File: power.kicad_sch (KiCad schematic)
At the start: 5 parts, among them U3 TCR2EF36, U4 MIC5365-3.0YD5-TR

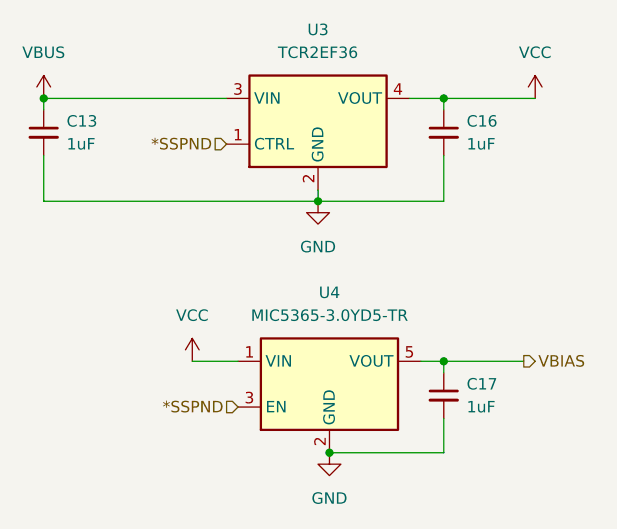
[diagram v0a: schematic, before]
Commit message: Add missing PCM2906 components; Partially Implement PCB
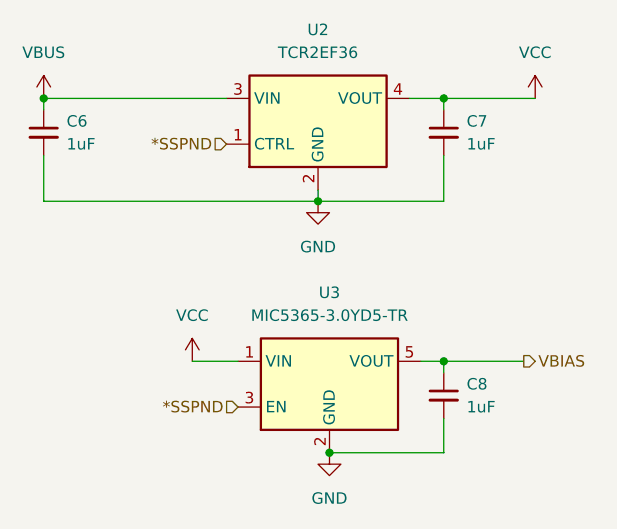
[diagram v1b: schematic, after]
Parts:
- C6: renamed from C13; footprint (none) -> Capacitor_SMD:C_0603_1608Metric_Pad1.08x0.95mm_HandSolder
- C7: renamed from C16; footprint (none) -> Capacitor_SMD:C_0603_1608Metric_Pad1.08x0.95mm_HandSolder
- C8: renamed from C17; footprint (none) -> Capacitor_SMD:C_0603_1608Metric_Pad1.08x0.95mm_HandSolder
- renumbered U3 to U2, U4 to U3
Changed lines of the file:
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@@
 		(dnp no)
 		(fields_autoplaced yes)
-		(property "Reference" "U3"
+		(property "Reference" "U2"
 			(at 132.08 92.71 0)
 			(effects
@@
 			(project ""
 				(path "/eb1afd54-626c-4526-850f-b0511eb9dc59/b6fbeffe-7e55-4f10-a8ab-72b4928b7916"
-					(reference "U3")
+					(reference "U2")
 					(unit 1)
 				)
@@
 		(dnp no)
 		(fields_autoplaced yes)
-		(property "Reference" "#PWR08"
+		(property "Reference" "#PWR07"
 			(at 118.11 133.35 0)
 			(effects
@@
 			(project ""
 				(path "/eb1afd54-626c-4526-850f-b0511eb9dc59/b6fbeffe-7e55-4f10-a8ab-72b4928b7916"
-					(reference "#PWR08")
+					(reference "#PWR07")
 					(unit 1)
 				)
@@
 		(dnp no)
 		(fields_autoplaced yes)
-		(property "Reference" "U4"
+		(property "Reference" "U3"
 			(at 133.35 121.92 0)
 			(effects
@@
 			(project ""
 				(path "/eb1afd54-626c-4526-850f-b0511eb9dc59/b6fbeffe-7e55-4f10-a8ab-72b4928b7916"
-					(reference "U4")
+					(reference "U3")
 					(unit 1)
 				)
@@
 		(dnp no)
 		(fields_autoplaced yes)
-		(property "Reference" "C13"
+		(property "Reference" "C6"
 			(at 104.14 102.8762 0)
 			(effects
@@
 			)
 		)
-		(property "Footprint" ""
+		(property "Footprint" "Capacitor_SMD:C_0603_1608Metric_Pad1.08x0.95mm_HandSolder"
 			(at 101.6 104.14 0)
 			(effects
@@
 			(project "lesson2"
 				(path "/eb1afd54-626c-4526-850f-b0511eb9dc59/b6fbeffe-7e55-4f10-a8ab-72b4928b7916"
-					(reference "C13")
+					(reference "C6")
 					(unit 1)
 				)
@@
 		(dnp no)
 		(fields_autoplaced yes)
-		(property "Reference" "C17"
+		(property "Reference" "C8"
 			(at 148.59 132.0862 0)
 			(effects
@@
 			)
 		)
-		(property "Footprint" ""
+		(property "Footprint" "Capacitor_SMD:C_0603_1608Metric_Pad1.08x0.95mm_HandSolder"
 			(at 146.05 133.35 0)
 			(effects
@@
 			(project ""
 				(path "/eb1afd54-626c-4526-850f-b0511eb9dc59/b6fbeffe-7e55-4f10-a8ab-72b4928b7916"
-					(reference "C17")
+					(reference "C8")
 					(unit 1)
 				)
@@
 		(dnp no)
 		(fields_autoplaced yes)
-		(property "Reference" "C16"
+		(property "Reference" "C7"
 			(at 148.59 102.8762 0)
 			(effects
@@
 			)
 		)
-		(property "Footprint" ""
+		(property "Footprint" "Capacitor_SMD:C_0603_1608Metric_Pad1.08x0.95mm_HandSolder"
 			(at 146.05 104.14 0)
 			(effects
@@
 			(project "lesson2"
 				(path "/eb1afd54-626c-4526-850f-b0511eb9dc59/b6fbeffe-7e55-4f10-a8ab-72b4928b7916"
-					(reference "C16")
+					(reference "C7")
 					(unit 1)
 				)
@@
 		(dnp no)
 		(fields_autoplaced yes)
-		(property "Reference" "#PWR07"
+		(property "Reference" "#PWR09"
 			(at 133.35 146.05 0)
 			(effects
@@
 			(project ""
 				(path "/eb1afd54-626c-4526-850f-b0511eb9dc59/b6fbeffe-7e55-4f10-a8ab-72b4928b7916"
-					(reference "#PWR07")
+					(reference "#PWR09")
 					(unit 1)
 				)
@@
 		(dnp no)
 		(fields_autoplaced yes)
-		(property "Reference" "#PWR09"
+		(property "Reference" "#PWR08"
 			(at 132.08 118.11 0)
 			(effects
@@
 			(project "lesson2"
 				(path "/eb1afd54-626c-4526-850f-b0511eb9dc59/b6fbeffe-7e55-4f10-a8ab-72b4928b7916"
-					(reference "#PWR09")
+					(reference "#PWR08")
 					(unit 1)
 				)
@@
 		(dnp no)
 		(fields_autoplaced yes)
-		(property "Reference" "#PWR011"
+		(property "Reference" "#PWR06"
 			(at 101.6 104.14 0)
 			(effects
@@
 			(project ""
 				(path "/eb1afd54-626c-4526-850f-b0511eb9dc59/b6fbeffe-7e55-4f10-a8ab-72b4928b7916"
-					(reference "#PWR011")
-					(unit 1)
-				)
+					(reference "#PWR06")
+					(unit 1)
+				)

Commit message: Correct PCB; Correct Root sheet; add PCB and 3D View pictures
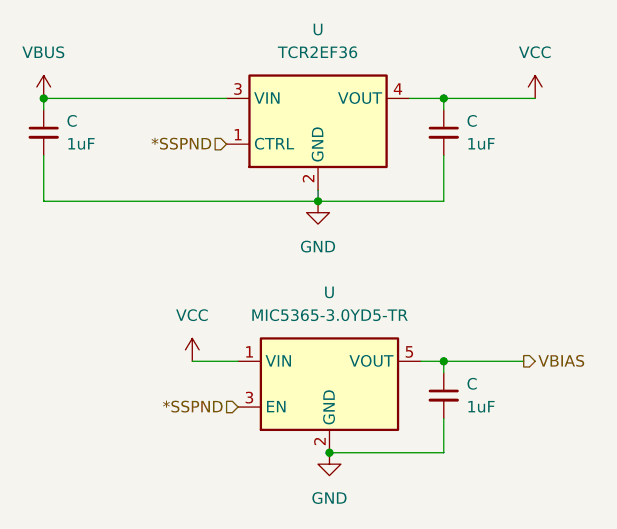
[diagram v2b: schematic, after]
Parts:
- renumbered C6 to C, C8 to C, C7 to C, U2 to U, U3 to U
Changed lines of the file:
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@@
 		(title "Power")
 		(date "2025-05-26")
-		(rev "0.1")
+		(rev "0.3")
 		(company "Maksym Rybalskyi <Maxdespairon@gmail.com>")
 	)
@@
 		(dnp no)
 		(fields_autoplaced yes)
-		(property "Reference" "U2"
+		(property "Reference" "U"
 			(at 132.08 92.71 0)
 			(effects
@@
 		(pin "4"
 		)
-		(instances
-			(project ""
-				(path "/eb1afd54-626c-4526-850f-b0511eb9dc59/b6fbeffe-7e55-4f10-a8ab-72b4928b7916"
-					(reference "U2")
-					(unit 1)
-				)
-			)
-		)
+		(instances)
 	)
 	(symbol
@@
 		(dnp no)
 		(fields_autoplaced yes)
-		(property "Reference" "#PWR07"
+		(property "Reference" "#PWR"
 			(at 118.11 133.35 0)
 			(effects
@@
 		(pin "1"
 		)
-		(instances
-			(project ""
-				(path "/eb1afd54-626c-4526-850f-b0511eb9dc59/b6fbeffe-7e55-4f10-a8ab-72b4928b7916"
-					(reference "#PWR07")
-					(unit 1)
-				)
-			)
-		)
+		(instances)
 	)
 	(symbol
@@
 		(dnp no)
 		(fields_autoplaced yes)
-		(property "Reference" "#PWR010"
+		(property "Reference" "#PWR"
 			(at 156.21 104.14 0)
 			(effects
@@
 		(pin "1"
 		)
-		(instances
-			(project ""
-				(path "/eb1afd54-626c-4526-850f-b0511eb9dc59/b6fbeffe-7e55-4f10-a8ab-72b4928b7916"
-					(reference "#PWR010")
-					(unit 1)
-				)
-			)
-		)
+		(instances)
 	)
 	(symbol
@@
 		(dnp no)
 		(fields_autoplaced yes)
-		(property "Reference" "U3"
+		(property "Reference" "U"
 			(at 133.35 121.92 0)
 			(effects
@@
 		(pin "1"
 		)
-		(instances
-			(project ""
-				(path "/eb1afd54-626c-4526-850f-b0511eb9dc59/b6fbeffe-7e55-4f10-a8ab-72b4928b7916"
-					(reference "U3")
-					(unit 1)
-				)
-			)
-		)
+		(instances)
 	)
 	(symbol
@@
 		(dnp no)
 		(fields_autoplaced yes)
-		(property "Reference" "C6"
+		(property "Reference" "C"
 			(at 104.14 102.8762 0)
 			(effects
@@
 		(pin "1"
 		)
-		(instances
-			(project "lesson2"
-				(path "/eb1afd54-626c-4526-850f-b0511eb9dc59/b6fbeffe-7e55-4f10-a8ab-72b4928b7916"
-					(reference "C6")
-					(unit 1)
-				)
-			)
-		)
+		(instances)
 	)
 	(symbol
@@
 		(dnp no)
 		(fields_autoplaced yes)
-		(property "Reference" "C8"
+		(property "Reference" "C"
 			(at 148.59 132.0862 0)
 			(effects
@@
 		(pin "1"
 		)
-		(instances
-			(project ""
-				(path "/eb1afd54-626c-4526-850f-b0511eb9dc59/b6fbeffe-7e55-4f10-a8ab-72b4928b7916"
-					(reference "C8")
-					(unit 1)
-				)
-			)
-		)
+		(instances)
 	)
 	(symbol
@@
 		(dnp no)
 		(fields_autoplaced yes)
-		(property "Reference" "C7"
+		(property "Reference" "C"
 			(at 148.59 102.8762 0)
 			(effects
@@
 		(pin "1"
 		)
-		(instances
-			(project "lesson2"
-				(path "/eb1afd54-626c-4526-850f-b0511eb9dc59/b6fbeffe-7e55-4f10-a8ab-72b4928b7916"
-					(reference "C7")
-					(unit 1)
-				)
-			)
-		)
+		(instances)
 	)
 	(symbol
@@
 		(dnp no)
 		(fields_autoplaced yes)
-		(property "Reference" "#PWR09"
+		(property "Reference" "#PWR"
 			(at 133.35 146.05 0)
 			(effects
@@
 		(pin "1"
 		)
-		(instances
-			(project ""
-				(path "/eb1afd54-626c-4526-850f-b0511eb9dc59/b6fbeffe-7e55-4f10-a8ab-72b4928b7916"
-					(reference "#PWR09")
-					(unit 1)
-				)
-			)
-		)
+		(instances)
 	)
 	(symbol
@@
 		(dnp no)
 		(fields_autoplaced yes)
-		(property "Reference" "#PWR08"
+		(property "Reference" "#PWR"
 			(at 132.08 118.11 0)
 			(effects
@@
 		(pin "1"
 		)
-		(instances
-			(project "lesson2"
-				(path "/eb1afd54-626c-4526-850f-b0511eb9dc59/b6fbeffe-7e55-4f10-a8ab-72b4928b7916"
-					(reference "#PWR08")
-					(unit 1)
-				)
-			)
-		)
+		(instances)
 	)
 	(symbol
@@
 		(dnp no)
 		(fields_autoplaced yes)
-		(property "Reference" "#PWR06"
+		(property "Reference" "#PWR"
 			(at 101.6 104.14 0)
 			(effects
@@
 		(pin "1"
 		)
-		(instances
-			(project ""
-				(path "/eb1afd54-626c-4526-850f-b0511eb9dc59/b6fbeffe-7e55-4f10-a8ab-72b4928b7916"
-					(reference "#PWR06")
-					(unit 1)
-				)
-			)
-		)
+		(instances)
 	)
 )
